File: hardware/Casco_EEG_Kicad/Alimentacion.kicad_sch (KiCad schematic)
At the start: 43 parts, among them J15 USB4125-GF-A_REVA2, Q1 FS8205A, SW2 PCM12SMTR, U4 TP4056-42-ESOP8, U5 DW01A, U7 AP2112K-3.3TRG1

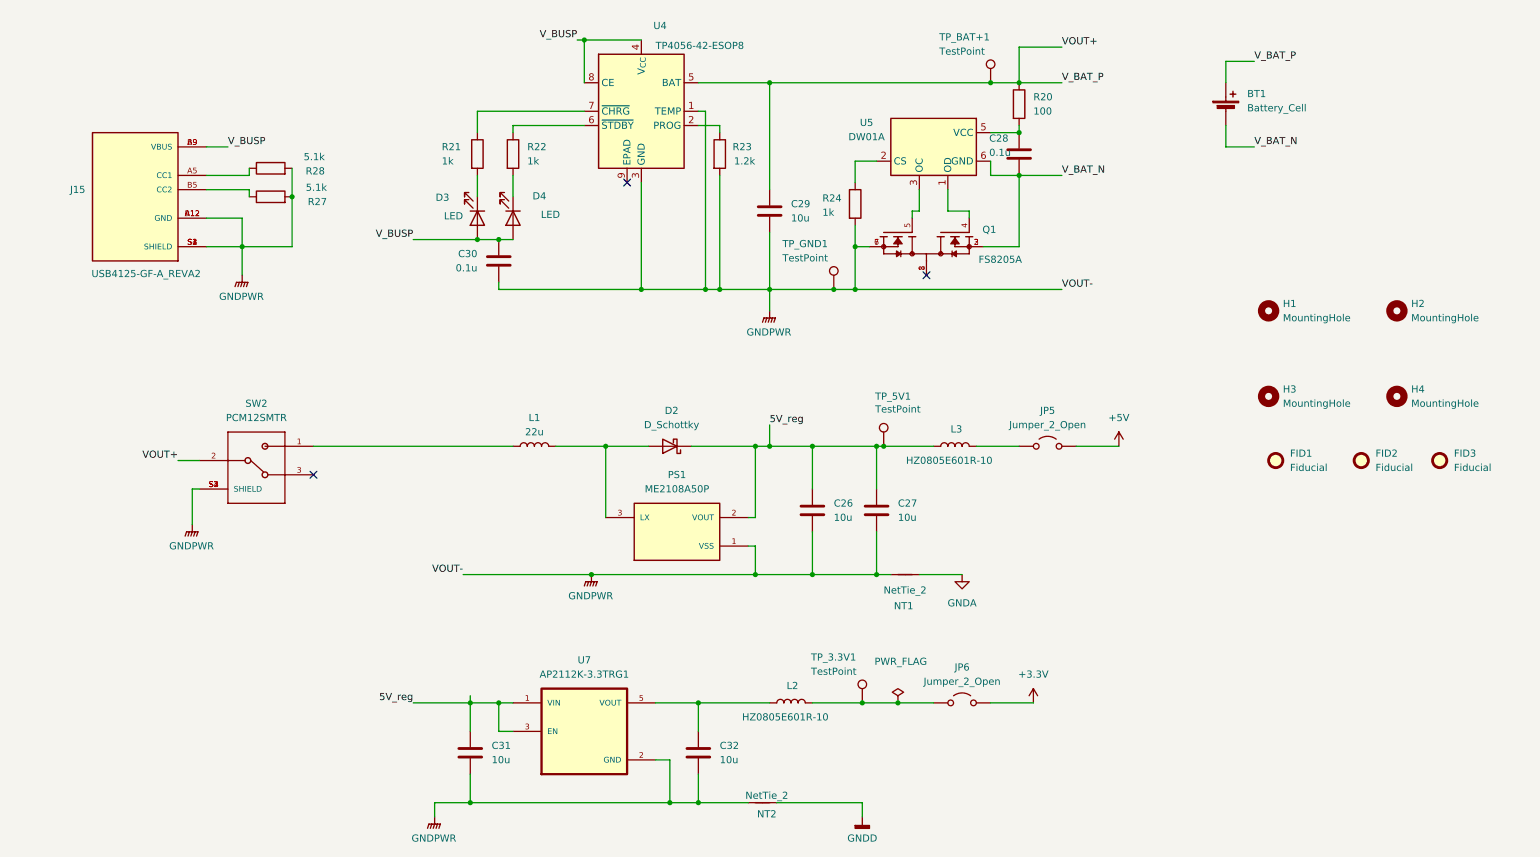
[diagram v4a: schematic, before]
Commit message: Agrego protecciones a las entradas analogicas, quito jumpers dealimentacion, agrego capacitores al HC05
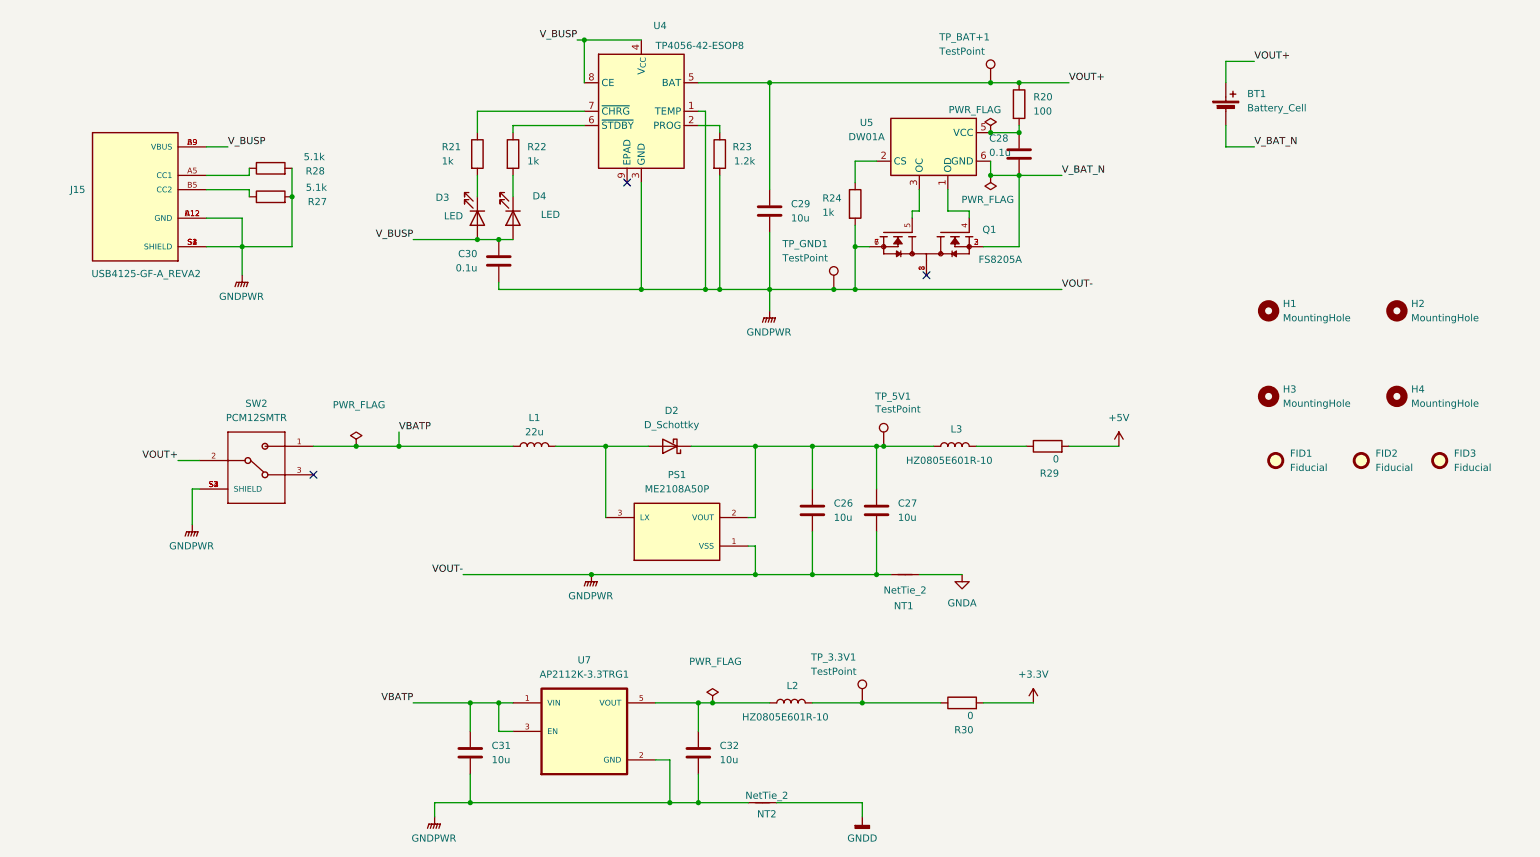
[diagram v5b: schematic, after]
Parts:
- removed JP5, JP6: Jumper_2_Open, Connector_PinHeader_2.54mm:PinHeader_1x02_P2.54mm_Vertical, symbol Jumper:Jumper_2_Open
- added R29, R30: 0, Resistor_SMD:R_0603_1608Metric, symbol Device:R
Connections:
- net +3.3V: now also R30.2
- net +5V: now also R29.2
- net at L3.2: now also R29.1
- net at L2.2, TP_3.3V1.1: now also R30.1
- net VBATP: now reaches L1.1, SW2.1
- net VBATP: now also C31.1, U7.1 (VIN), U7.3 (EN)
- net 5V_reg: no longer names the net of C26.1, C27.1, D2.1 (K), L3.1, PS1.2 (VOUT), TP_5V1.1
- net 5V_reg: no longer C31.1, U7.1 (VIN), U7.3 (EN)

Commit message: Cambio jumpers
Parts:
- removed R29, R30: 0, Resistor_SMD:R_0603_1608Metric, symbol Device:R
- added JP5, JP6: Jumper_2_Open, Jumper:SolderJumper-2_P1.3mm_Open_RoundedPad1.0x1.5mm, symbol Jumper:Jumper_2_Open
- R27, R28: LCSC PN C21190 -> C23186
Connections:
- net +3.3V: now also JP6.2 (B)
- net +5V: now also JP5.2 (B)
- net at L3.2: now also JP5.1 (A)
- net at L2.2, TP_3.3V1.1: now also JP6.1 (A)
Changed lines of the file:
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@@
 	(wire
 		(pts
+			(xy 200.66 97.79) (xy 207.01 97.79)
+		)
+		(stroke
+			(width 0)
+			(type default)
+		)
+	)
+	(wire
+		(pts
 			(xy 170.18 55.88) (xy 170.18 57.15)
 		)
@@
 	(wire
 		(pts
-			(xy 182.88 143.51) (xy 191.77 143.51)
+			(xy 124.46 143.51) (xy 132.08 143.51)
 		)
 		(stroke
@@
 	(wire
 		(pts
-			(xy 124.46 143.51) (xy 132.08 143.51)
+			(xy 156.21 69.85) (xy 160.02 69.85)
 		)
 		(stroke
@@
 	(wire
 		(pts
-			(xy 156.21 69.85) (xy 160.02 69.85)
+			(xy 160.02 62.23) (xy 160.02 69.85)
 		)
 		(stroke
@@
 	(wire
 		(pts
-			(xy 160.02 62.23) (xy 160.02 69.85)
+			(xy 132.08 38.1) (xy 133.35 38.1)
 		)
 		(stroke
@@
 	(wire
 		(pts
-			(xy 132.08 38.1) (xy 133.35 38.1)
+			(xy 185.42 143.51) (xy 191.77 143.51)
 		)
 		(stroke
@@
 	(wire
 		(pts
-			(xy 198.12 97.79) (xy 207.01 97.79)
-		)
-		(stroke
-			(width 0)
-			(type default)
-		)
-	)
-	(wire
-		(pts
 			(xy 59.69 62.23) (xy 50.8 62.23)
 		)
@@
 			)
 		)
-		(property "LCSC PN" "C21190"
+		(property "LCSC PN" "C23186"
 			(at 55.88 53.34 0)
 			(effects
@@
 	)
 	(symbol
-		(lib_id "Device:R")
-		(at 194.31 97.79 90)
-		(unit 1)
-		(exclude_from_sim no)
-		(in_bom yes)
-		(on_board yes)
-		(dnp no)
-		(property "Reference" "R29"
-			(at 196.342 102.616 90)
-			(effects
-				(font
-					(size 1.27 1.27)
-				)
-				(justify left)
-			)
-		)
-		(property "Value" "0"
-			(at 196.342 100.076 90)
-			(effects
-				(font
-					(size 1.27 1.27)
-				)
-				(justify left)
-			)
-		)
-		(property "Footprint" "Resistor_SMD:R_0603_1608Metric"
-			(at 194.31 99.568 90)
-			(effects
-				(font
-					(size 1.27 1.27)
-				)
-				(hide yes)
-			)
-		)
-		(property "Datasheet" "~"
-			(at 194.31 97.79 0)
-			(effects
-				(font
-					(size 1.27 1.27)
-				)
-				(hide yes)
-			)
-		)
-		(property "Description" "Resistor"
-			(at 194.31 97.79 0)
-			(effects
-				(font
-					(size 1.27 1.27)
-				)
-				(hide yes)
-			)
-		)
-		(property "LCSC PN" "C21190"
-			(at 194.31 97.79 0)
-			(effects
-				(font
-					(size 1.27 1.27)
-				)
-				(hide yes)
-			)
-		)
-		(pin "1"
-		)
-		(pin "2"
-		)
-		(instances
-			(project "Casco_EEG_Kicad"
-				(path "/3414db36-80da-469c-8b48-81d6bd2f8966/738a2f03-0f5c-435b-af80-cc097a0ed5f5"
-					(reference "R29")
-					(unit 1)
-				)
-			)
-		)
-	)
-	(symbol
 		(lib_id "power:GNDPWR")
 		(at 85.09 163.83 0)
@@
 	)
 	(symbol
-		(lib_id "Device:R")
-		(at 179.07 143.51 90)
-		(unit 1)
-		(exclude_from_sim no)
-		(in_bom yes)
-		(on_board yes)
-		(dnp no)
-		(property "Reference" "R30"
-			(at 181.102 148.336 90)
-			(effects
-				(font
-					(size 1.27 1.27)
-				)
-				(justify left)
-			)
-		)
-		(property "Value" "0"
-			(at 181.102 145.796 90)
-			(effects
-				(font
-					(size 1.27 1.27)
-				)
-				(justify left)
-			)
-		)
-		(property "Footprint" "Resistor_SMD:R_0603_1608Metric"
-			(at 179.07 145.288 90)
-			(effects
-				(font
-					(size 1.27 1.27)
-				)
-				(hide yes)
-			)
-		)
-		(property "Datasheet" "~"
-			(at 179.07 143.51 0)
-			(effects
-				(font
-					(size 1.27 1.27)
-				)
-				(hide yes)
-			)
-		)
-		(property "Description" "Resistor"
-			(at 179.07 143.51 0)
-			(effects
-				(font
-					(size 1.27 1.27)
-				)
-				(hide yes)
-			)
-		)
-		(property "LCSC PN" "C21190"
-			(at 179.07 143.51 0)
-			(effects
-				(font
-					(size 1.27 1.27)
-				)
-				(hide yes)
-			)
-		)
-		(pin "1"
-		)
-		(pin "2"
-		)
-		(instances
-			(project "Casco_EEG_Kicad"
-				(path "/3414db36-80da-469c-8b48-81d6bd2f8966/738a2f03-0f5c-435b-af80-cc097a0ed5f5"
-					(reference "R30")
-					(unit 1)
-				)
-			)
-		)
-	)
-	(symbol
 		(lib_id "power:PWR_FLAG")
 		(at 134.62 143.51 0)
@@
 			)
 		)
-		(property "LCSC PN" "C21190"
+		(property "LCSC PN" "C23186"
 			(at 55.88 48.26 0)
 			(effects
@@
 					(unit 1)
 				)
+			)
+		)
+	)
+	(symbol
+		(lib_id "Jumper:Jumper_2_Open")
+		(at 195.58 97.79 0)
+		(unit 1)
+		(exclude_from_sim no)
+		(in_bom yes)
+		(on_board yes)
+		(dnp no)
+		(fields_autoplaced yes)
+		(property "Reference" "JP5"
+			(at 195.58 91.44 0)
+			(effects
+				(font
+					(size 1.27 1.27)
+				)
+			)
+		)
+		(property "Value" "Jumper_2_Open"
+			(at 195.58 93.98 0)
+			(effects
+				(font
+					(size 1.27 1.27)
+				)
+			)
+		)
+		(property "Footprint" "Jumper:SolderJumper-2_P1.3mm_Open_RoundedPad1.0x1.5mm"
+			(at 195.58 97.79 0)
+			(effects
+				(font
+					(size 1.27 1.27)
+				)
+				(hide yes)
+			)
+		)
+		(property "Datasheet" "~"
+			(at 195.58 97.79 0)
+			(effects
+				(font
+					(size 1.27 1.27)
+				)
+				(hide yes)
+			)
+		)
+		(property "Description" "Jumper, 2-pole, open"
+			(at 195.58 97.79 0)
+			(effects
+				(font
+					(size 1.27 1.27)
+				)
+				(hide yes)
+			)
+		)
+		(pin "1"
+		)
+		(pin "2"
+		)
+		(instances
+			(project ""
+				(path "/3414db36-80da-469c-8b48-81d6bd2f8966/738a2f03-0f5c-435b-af80-cc097a0ed5f5"
+					(reference "JP5")
+					(unit 1)
+				)
+			)
+		)
+	)
+	(symbol
+		(lib_id "Jumper:Jumper_2_Open")
+		(at 180.34 143.51 0)
+		(unit 1)
+		(exclude_from_sim no)
+		(in_bom yes)
+		(on_board yes)
+		(dnp no)
+		(fields_autoplaced yes)
+		(property "Reference" "JP6"
+			(at 180.34 137.16 0)
+			(effects
+				(font
+					(size 1.27 1.27)
+				)
+			)
+		)
+		(property "Value" "Jumper_2_Open"
+			(at 180.34 139.7 0)
+			(effects
+				(font
+					(size 1.27 1.27)
+				)
+			)
+		)
+		(property "Footprint" "Jumper:SolderJumper-2_P1.3mm_Open_RoundedPad1.0x1.5mm"
+			(at 180.34 143.51 0)
+			(effects
+				(font
+					(size 1.27 1.27)
+				)
+				(hide yes)
+			)
+		)
+		(property "Datasheet" "~"
+			(at 180.34 143.51 0)
+			(effects
+				(font
+					(size 1.27 1.27)
+				)
+				(hide yes)
+			)
+		)
+		(property "Description" "Jumper, 2-pole, open"
+			(at 180.34 143.51 0)
+			(effects
+				(font
+					(size 1.27 1.27)
+				)
+				(hide yes)
+			)
+		)
+		(pin "1"
+		)
+		(pin "2"
+		)
+		(instances
+			(project "Casco_EEG_Kicad"
+				(path "/3414db36-80da-469c-8b48-81d6bd2f8966/738a2f03-0f5c-435b-af80-cc097a0ed5f5"
+					(reference "JP6")
+					(unit 1)
+				)

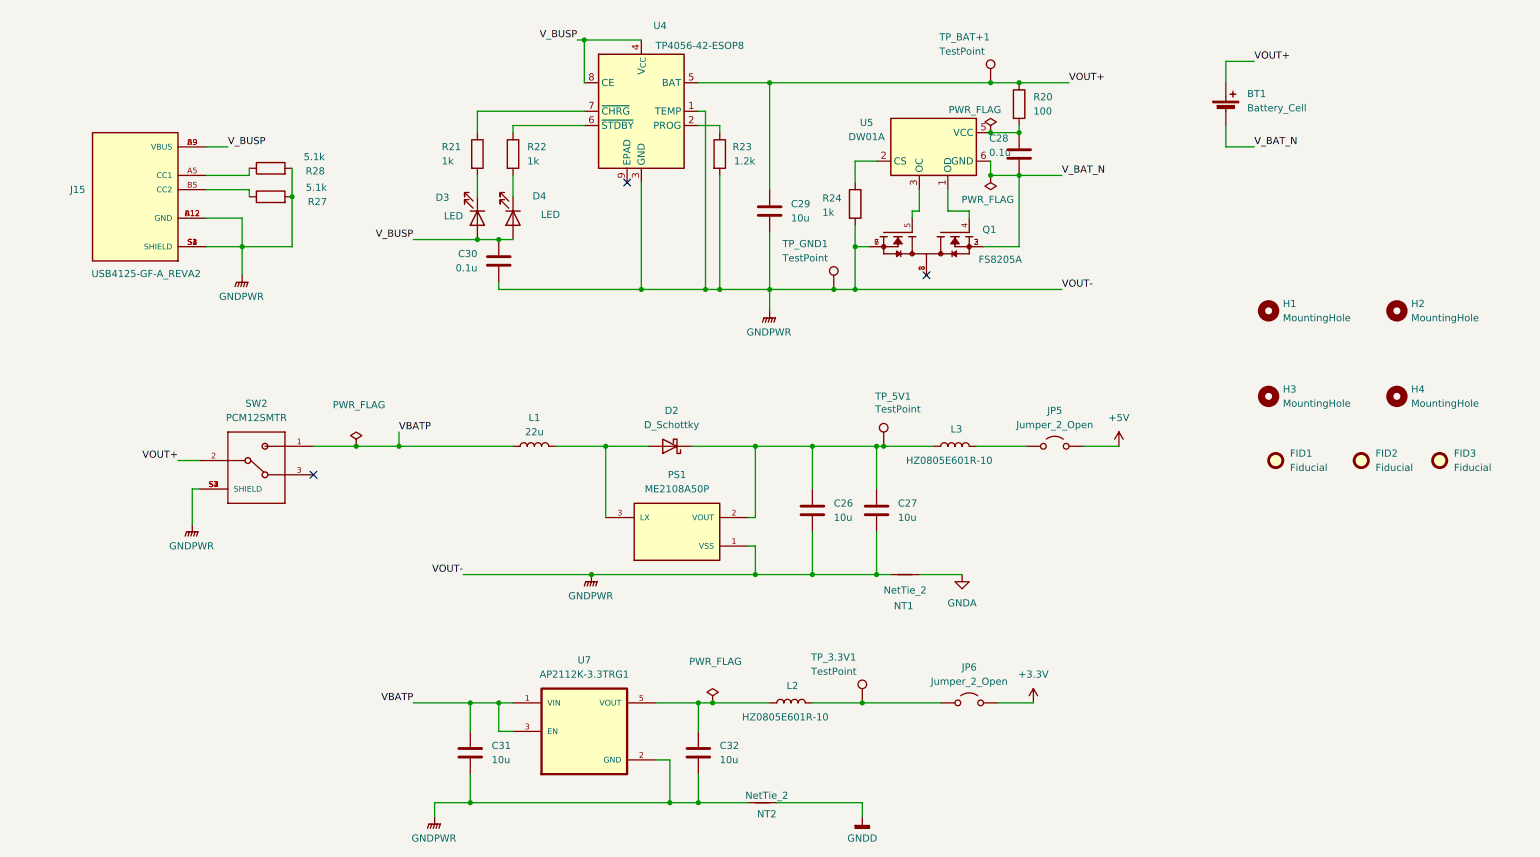
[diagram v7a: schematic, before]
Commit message: Actualización de pcb con aislamiento dc/dc, elimino entradas de trigger
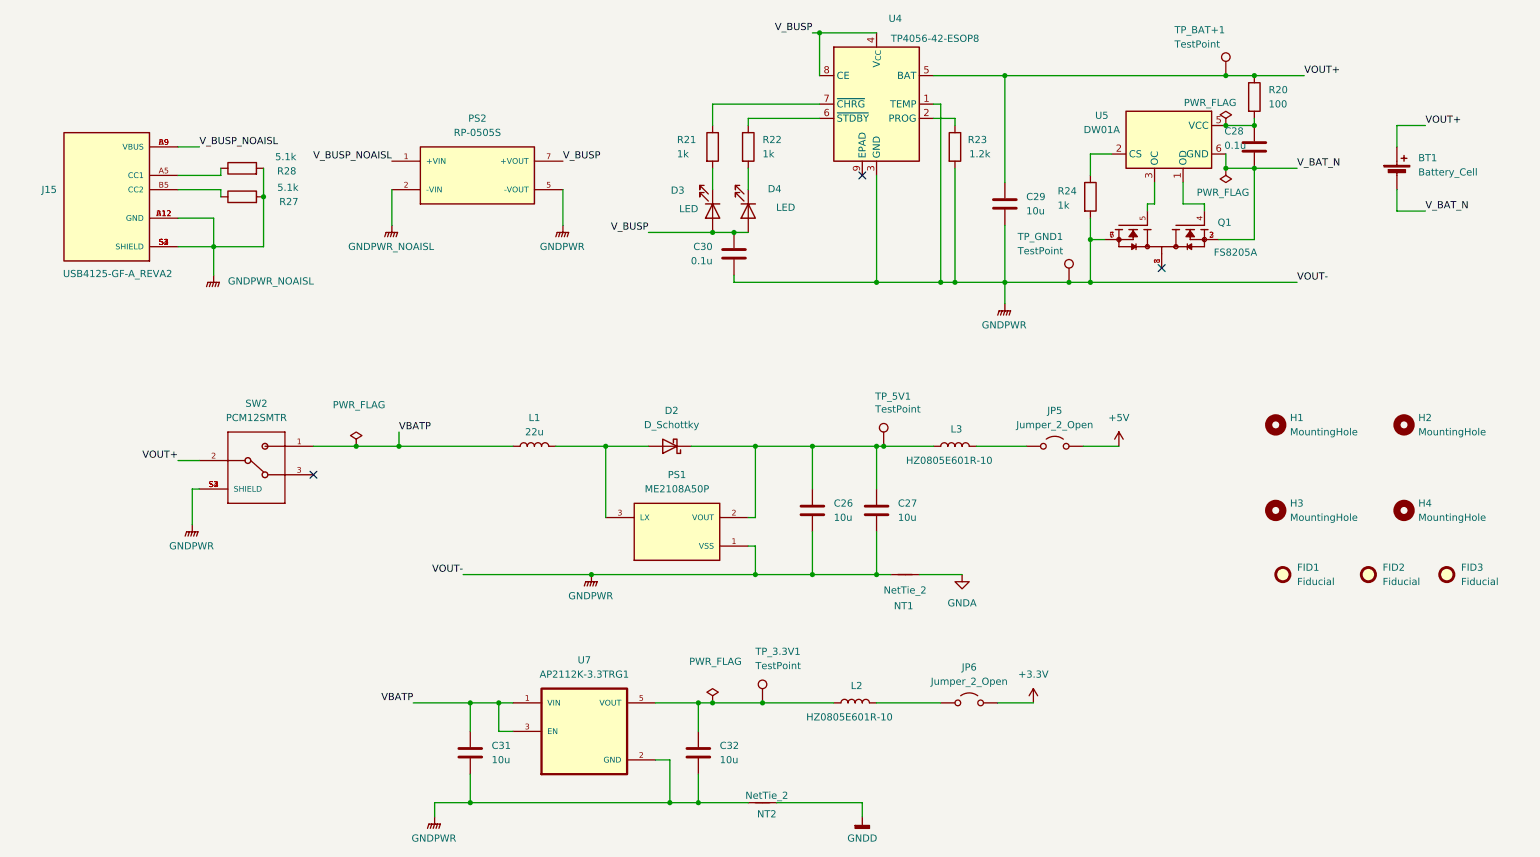
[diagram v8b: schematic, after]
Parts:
- added PS2: RP-0505S, Huellas:CONV_RP-0505S, symbol RP0505:RP-0505S
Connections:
- net GNDPWR: now also PS2.5 (-VOUT); no longer J15.A12 (GND), J15.B12 (GND), J15.S1 (SHIELD), J15.S2 (SHIELD), J15.S3 (SHIELD), J15.S4 (SHIELD), R27.2, R28.2
- net V_BUSP: now also PS2.7 (+VOUT); no longer J15.A9 (VBUS), J15.B9 (VBUS)
- net at C32.1, L2.1, U7.5 (VOUT): now also TP_3.3V1.1
- net at JP6.1 (A), L2.2: no longer TP_3.3V1.1
- new net GNDPWR_NOAISL: J15.A12 (GND), J15.B12 (GND), J15.S1 (SHIELD), J15.S2 (SHIELD), J15.S3 (SHIELD), J15.S4 (SHIELD), PS2.2 (-VIN), R27.2, R28.2
- new net V_BUSP_NOAISL: J15.A9 (VBUS), J15.B9 (VBUS), PS2.1 (+VIN)
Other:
- moved on the sheet: BT1, C28, C29, C30, D3, D4, FID1, FID2, FID3, H1, H2, H3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
